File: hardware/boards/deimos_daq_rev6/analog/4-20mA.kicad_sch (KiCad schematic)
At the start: 6 parts, among them IC24001 BD42540FJ-CE2

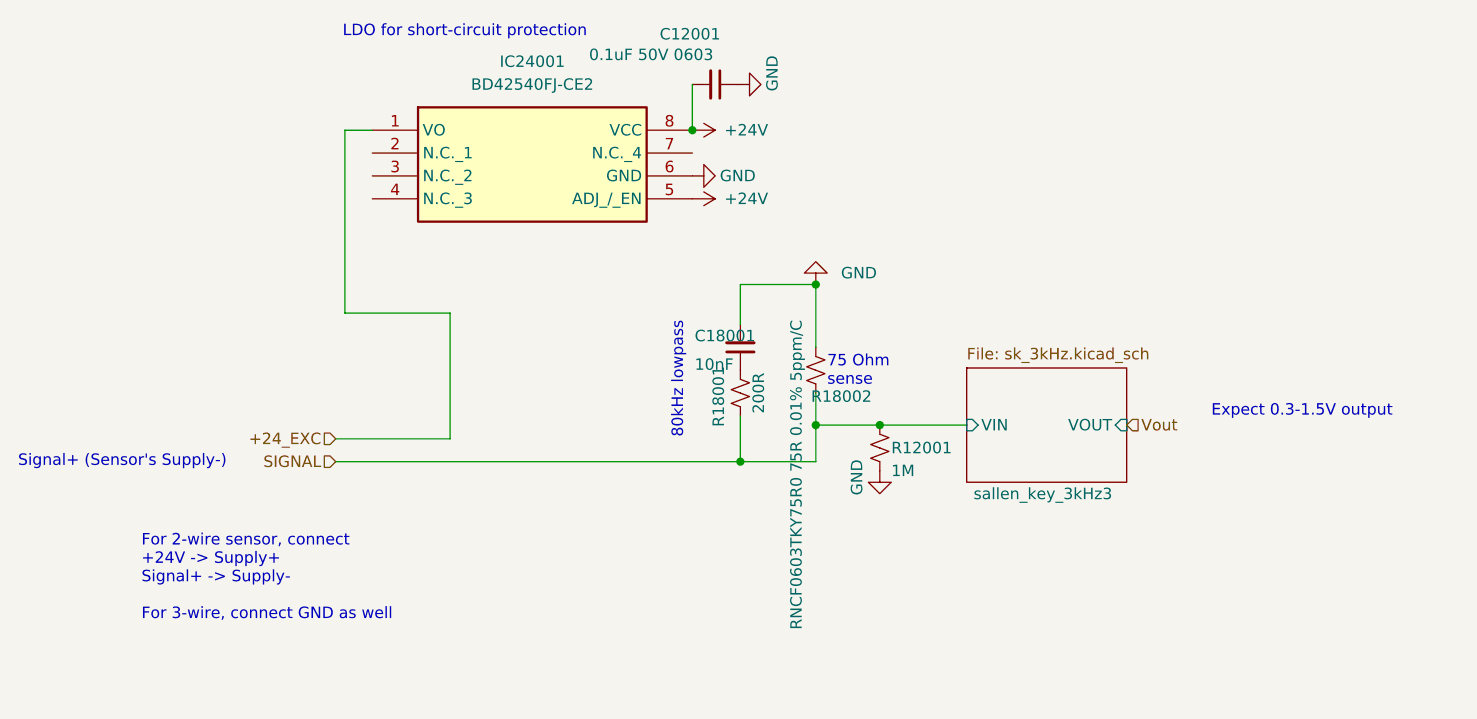
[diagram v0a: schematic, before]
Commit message: exclude testpoints from BOM
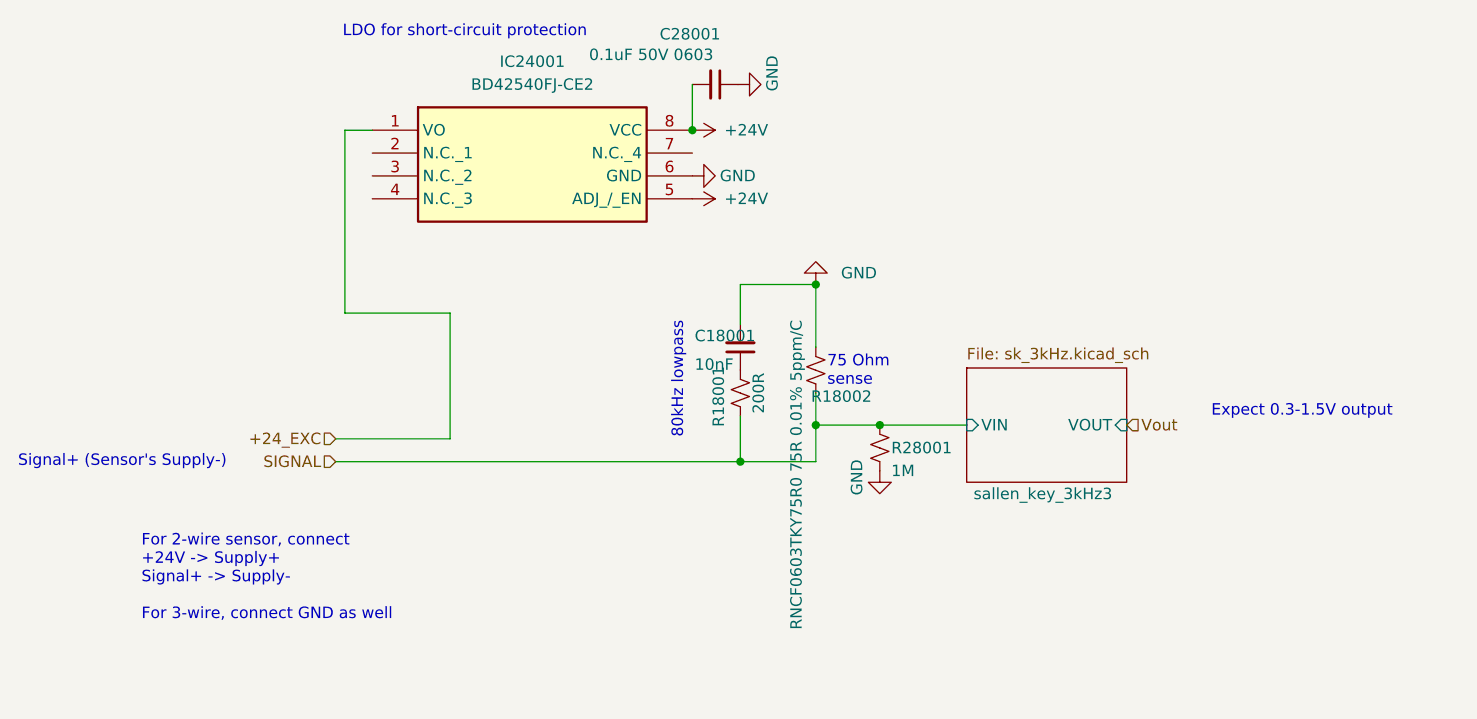
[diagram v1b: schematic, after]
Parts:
- renumbered C12001 to C28001, R12001 to R28001
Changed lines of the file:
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@@
 		(on_board yes)
 		(dnp no)
-		(property "Reference" "#PWR12001"
+		(property "Reference" "#PWR251"
 			(at 141.732 112.776 0)
 			(effects
@@
 		)
 		(instances
+			(project "analog_i"
+				(path "/5a60c4b1-b6cb-416e-8883-8291fa089b87/c2baf18d-2b19-4edb-98b3-535275ee271f/77831b95-4af9-4be7-883d-350d130a19a2"
+					(reference "#PWR262")
+					(unit 1)
+				)
+				(path "/5a60c4b1-b6cb-416e-8883-8291fa089b87/c2baf18d-2b19-4edb-98b3-535275ee271f/b7e73f80-a01f-409c-a1ae-634c4b865833"
+					(reference "#PWR276")
+					(unit 1)
+				)
+				(path "/5a60c4b1-b6cb-416e-8883-8291fa089b87/c2baf18d-2b19-4edb-98b3-535275ee271f/c99c1b0b-6659-4cec-a152-edd7ebc08576"
+					(reference "#PWR299")
+					(unit 1)
+				)
+				(path "/5a60c4b1-b6cb-416e-8883-8291fa089b87/c2baf18d-2b19-4edb-98b3-535275ee271f/ed7a0d70-4012-4e50-88a7-aea647708582"
+					(reference "#PWR251")
+					(unit 1)
+				)
+			)
 			(project "analog_frontend_panel"
 				(path "/c241d083-1323-4b4a-a540-956d0afb7b72/77831b95-4af9-4be7-883d-350d130a19a2"
@@
 		(on_board yes)
 		(dnp no)
-		(property "Reference" "C12001"
+		(property "Reference" "C28001"
 			(at 120.65 57.912 90)
 			(effects
@@
 		)
 		(instances
+			(project "analog_i"
+				(path "/5a60c4b1-b6cb-416e-8883-8291fa089b87/c2baf18d-2b19-4edb-98b3-535275ee271f/77831b95-4af9-4be7-883d-350d130a19a2"
+					(reference "C30001")
+					(unit 1)
+				)
+				(path "/5a60c4b1-b6cb-416e-8883-8291fa089b87/c2baf18d-2b19-4edb-98b3-535275ee271f/b7e73f80-a01f-409c-a1ae-634c4b865833"
+					(reference "C32001")
+					(unit 1)
+				)
+				(path "/5a60c4b1-b6cb-416e-8883-8291fa089b87/c2baf18d-2b19-4edb-98b3-535275ee271f/c99c1b0b-6659-4cec-a152-edd7ebc08576"
+					(reference "C34001")
+					(unit 1)
+				)
+				(path "/5a60c4b1-b6cb-416e-8883-8291fa089b87/c2baf18d-2b19-4edb-98b3-535275ee271f/ed7a0d70-4012-4e50-88a7-aea647708582"
+					(reference "C28001")
+					(unit 1)
+				)
+			)
 			(project "analog_frontend_panel"
 				(path "/c241d083-1323-4b4a-a540-956d0afb7b72/77831b95-4af9-4be7-883d-350d130a19a2"
@@
 		(on_board yes)
 		(dnp no)
-		(property "Reference" "R12001"
+		(property "Reference" "R28001"
 			(at 143.002 103.886 0)
 			(effects
@@
 		)
 		(instances
+			(project "analog_i"
+				(path "/5a60c4b1-b6cb-416e-8883-8291fa089b87/c2baf18d-2b19-4edb-98b3-535275ee271f/77831b95-4af9-4be7-883d-350d130a19a2"
+					(reference "R30001")
+					(unit 1)
+				)
+				(path "/5a60c4b1-b6cb-416e-8883-8291fa089b87/c2baf18d-2b19-4edb-98b3-535275ee271f/b7e73f80-a01f-409c-a1ae-634c4b865833"
+					(reference "R32001")
+					(unit 1)
+				)
+				(path "/5a60c4b1-b6cb-416e-8883-8291fa089b87/c2baf18d-2b19-4edb-98b3-535275ee271f/c99c1b0b-6659-4cec-a152-edd7ebc08576"
+					(reference "R34001")
+					(unit 1)
+				)
+				(path "/5a60c4b1-b6cb-416e-8883-8291fa089b87/c2baf18d-2b19-4edb-98b3-535275ee271f/ed7a0d70-4012-4e50-88a7-aea647708582"
+					(reference "R28001")
+					(unit 1)
+				)
+			)
 			(project "analog_frontend_panel"
 				(path "/c241d083-1323-4b4a-a540-956d0afb7b72/77831b95-4af9-4be7-883d-350d130a19a2"
@@
 		(dnp no)
 		(fields_autoplaced yes)
-		(property "Reference" "#PWR12002"
+		(property "Reference" "#PWR247"
 			(at 117.094 76.2 0)
 			(effects
@@
 		)
 		(instances
+			(project "analog_i"
+				(path "/5a60c4b1-b6cb-416e-8883-8291fa089b87/c2baf18d-2b19-4edb-98b3-535275ee271f/77831b95-4af9-4be7-883d-350d130a19a2"
+					(reference "#PWR260")
+					(unit 1)
+				)
+				(path "/5a60c4b1-b6cb-416e-8883-8291fa089b87/c2baf18d-2b19-4edb-98b3-535275ee271f/b7e73f80-a01f-409c-a1ae-634c4b865833"
+					(reference "#PWR273")
+					(unit 1)
+				)
+				(path "/5a60c4b1-b6cb-416e-8883-8291fa089b87/c2baf18d-2b19-4edb-98b3-535275ee271f/c99c1b0b-6659-4cec-a152-edd7ebc08576"
+					(reference "#PWR292")
+					(unit 1)
+				)
+				(path "/5a60c4b1-b6cb-416e-8883-8291fa089b87/c2baf18d-2b19-4edb-98b3-535275ee271f/ed7a0d70-4012-4e50-88a7-aea647708582"
+					(reference "#PWR247")
+					(unit 1)
+				)
+			)
 			(project "analog_frontend_panel"
 				(path "/c241d083-1323-4b4a-a540-956d0afb7b72/77831b95-4af9-4be7-883d-350d130a19a2"
@@
 		(on_board yes)
 		(dnp no)
-		(property "Reference" "#PWR12003"
+		(property "Reference" "#PWR248"
 			(at 132.334 63.5 0)
 			(effects
@@
 		)
 		(instances
+			(project "analog_i"
+				(path "/5a60c4b1-b6cb-416e-8883-8291fa089b87/c2baf18d-2b19-4edb-98b3-535275ee271f/77831b95-4af9-4be7-883d-350d130a19a2"
+					(reference "#PWR261")
+					(unit 1)
+				)
+				(path "/5a60c4b1-b6cb-416e-8883-8291fa089b87/c2baf18d-2b19-4edb-98b3-535275ee271f/b7e73f80-a01f-409c-a1ae-634c4b865833"
+					(reference "#PWR275")
+					(unit 1)
+				)
+				(path "/5a60c4b1-b6cb-416e-8883-8291fa089b87/c2baf18d-2b19-4edb-98b3-535275ee271f/c99c1b0b-6659-4cec-a152-edd7ebc08576"
+					(reference "#PWR297")
+					(unit 1)
+				)
+				(path "/5a60c4b1-b6cb-416e-8883-8291fa089b87/c2baf18d-2b19-4edb-98b3-535275ee271f/ed7a0d70-4012-4e50-88a7-aea647708582"
+					(reference "#PWR248")
+					(unit 1)
+				)
+			)
 			(project "analog_frontend_panel"
 				(path "/c241d083-1323-4b4a-a540-956d0afb7b72/77831b95-4af9-4be7-883d-350d130a19a2"
